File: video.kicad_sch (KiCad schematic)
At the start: 36 parts, among them CN10 COMPOSITE, CN9 VIDEO_DB23M, U4 DENISE, U40 74LS245, U41 74LS245, U94 74HCT14

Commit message: DRAM chips replaced with SIMM module
Added logic to decode 2MB chip + 1.5MB slow
Rewired trapdoor slot
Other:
- title: Rämixx500 -> Rämixx500_max
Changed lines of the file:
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@@
 	(paper "A3")
 	(title_block
-		(title "Rämixx500")
-		(date "2021-05-22")
-		(rev "1")
+		(title "Rämixx500_max")
+		(date "2026-03-13")
+		(rev "2")
 		(company "SukkoPera")
 		(comment 1 "DENISE IS PRETTY MUCH INTO VIDEO...")

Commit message: Completed routing, no DRC errors (but still a lot of warnings)
TODO: thoroughly review all small schematic changes
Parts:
- JP11: now left out of the parts list
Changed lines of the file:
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@@
 	(title_block
 		(title "Rämixx500_max")
-		(date "2026-03-13")
-		(rev "2")
+		(date "2026-03-25")
+		(rev "3")
 		(company "SukkoPera")
 		(comment 1 "DENISE IS PRETTY MUCH INTO VIDEO...")
@@
 		(unit 1)
 		(exclude_from_sim no)
-		(in_bom yes)
+		(in_bom no)
 		(on_board yes)
 		(dnp no)

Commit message: Started cleaning up BOM
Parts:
- JP99H1, JP99V1: now left out of the parts list
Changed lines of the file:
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@@
 		(unit 1)
 		(exclude_from_sim no)
-		(in_bom yes)
+		(in_bom no)
 		(on_board yes)
 		(dnp no)
@@
 		(unit 1)
 		(exclude_from_sim no)
-		(in_bom yes)
+		(in_bom no)
 		(on_board yes)
 		(dnp no)

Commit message: Working on BOM
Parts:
- C4, C40, C41: MFG Part Num C412C334M5U5TA -> C440C334K5R5TA7200; Mouser (none) -> 80-C440C334K5R-TR
- C401, C402: MFG Part Num EEUFR1C102 -> ECA-1EM102; Mouser (none) -> 667-ECA-1EM102
- C403, HY2: now not fitted
- C94: MFG Name (none) -> VISHAY; MFG Part Num (none) -> A104K15X7RF5TAA; Mouser (none) -> 594-A104K15X7RF5TAA
- CN10: MFG Name (none) -> SWITCHCRAFT; MFG Part Num (none) -> PJRAN1X1U01AUX; Mouser (none) -> 502-PJRAN1X1U01AUX
- CN9: MFG Name (none) -> COMMODORE; MFG Part Num (none) -> 390242-03
- HY1: MFG Name SKIP -> COMMODORE; MFG Part Num SKIP -> 390229-03

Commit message: more work on BOM done
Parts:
- E406: Mouser (none) -> 81-DSS1NB32A103Q91A
- R402, R403, R404: MFG Name (none) -> YAGEO; MFG Part Num (none) -> MFR-25FBF52-4K7; Mouser (none) -> 603-MFR-25FBF52-4K7
- R405: MFG Name (none) -> VISHAY; MFG Part Num (none) -> PR02000204707JA100; Mouser (none) -> 594-PR02000204707JA1
- R406: MFG Name (none) -> VISHAY; MFG Part Num (none) -> PR02000204708JA100; Mouser (none) -> 594-5083NW4R700JA100
- R409: MFG Name (none) -> YAGEO; MFG Part Num (none) -> MFR-25FBF52-150R; Mouser (none) -> 603-MFR-25FBF52-150R
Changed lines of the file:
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@@
 			)
 		)
-		(property "Mouser" ""
+		(property "Mouser" "603-MFR-25FBF52-4K7 "
+			(at 293.751 197.104 90)
+			(effects
+				(font
+					(size 1.27 1.27)
+				)
+				(hide yes)
+			)
+		)
+		(property "MFG Name" "YAGEO"
+			(at 293.751 197.104 90)
+			(effects
+				(font
+					(size 1.27 1.27)
+				)
+				(hide yes)
+			)
+		)
+		(property "MFG Part Num" "MFR-25FBF52-4K7 "
 			(at 293.751 197.104 90)
 			(effects
@@
 			)
 		)
-		(property "Mouser" ""
+		(property "Mouser" " 81-DSS1NB32A103Q91A "
 			(at 87.63 182.88 0)
 			(effects
@@
 			)
 		)
-		(property "Mouser" ""
+		(property "Mouser" "603-MFR-25FBF52-4K7 "
+			(at 323.723 79.248 90)
+			(effects
+				(font
+					(size 1.27 1.27)
+				)
+				(hide yes)
+			)
+		)
+		(property "MFG Name" "YAGEO"
+			(at 323.723 79.248 90)
+			(effects
+				(font
+					(size 1.27 1.27)
+				)
+				(hide yes)
+			)
+		)
+		(property "MFG Part Num" "MFR-25FBF52-4K7 "
 			(at 323.723 79.248 90)
 			(effects
@@
 			)
 		)
-		(property "Mouser" ""
+		(property "Mouser" "603-MFR-25FBF52-4K7 "
+			(at 328.549 79.121 90)
+			(effects
+				(font
+					(size 1.27 1.27)
+				)
+				(hide yes)
+			)
+		)
+		(property "MFG Name" "YAGEO"
+			(at 328.549 79.121 90)
+			(effects
+				(font
+					(size 1.27 1.27)
+				)
+				(hide yes)
+			)
+		)
+		(property "MFG Part Num" "MFR-25FBF52-4K7 "
 			(at 328.549 79.121 90)
 			(effects
@@
 			)
 		)
-		(property "Mouser" ""
+		(property "Mouser" "594-5083NW4R700JA100"
+			(at 119.38 193.04 90)
+			(effects
+				(font
+					(size 1.27 1.27)
+				)
+				(hide yes)
+			)
+		)
+		(property "MFG Name" "VISHAY"
+			(at 119.38 193.04 90)
+			(effects
+				(font
+					(size 1.27 1.27)
+				)
+				(hide yes)
+			)
+		)
+		(property "MFG Part Num" "PR02000204708JA100 "
 			(at 119.38 193.04 90)
 			(effects
@@
 			)
 		)
-		(property "Mouser" ""
+		(property "Mouser" "594-PR02000204707JA1 "
+			(at 255.905 193.04 90)
+			(effects
+				(font
+					(size 1.27 1.27)
+				)
+				(hide yes)
+			)
+		)
+		(property "MFG Name" "VISHAY"
+			(at 255.905 193.04 90)
+			(effects
+				(font
+					(size 1.27 1.27)
+				)
+				(hide yes)
+			)
+		)
+		(property "MFG Part Num" "PR02000204707JA100"
 			(at 255.905 193.04 90)
 			(effects
@@
 			)
 		)
-		(property "Mouser" ""
+		(property "Mouser" "603-MFR-25FBF52-150R"
 			(at 247.396 106.553 0)
 			(effects
+				(font
+					(size 1.27 1.27)
+				)
+				(hide yes)
+			)
+		)
+		(property "MFG Name" "YAGEO"
+			(at 247.396 106.553 0)
+			(effects
+				(font
+					(size 1.27 1.27)
+				)
+				(hide yes)
+			)
+		)
+		(property "MFG Part Num" "MFR-25FBF52-150R"
+			(at 247.396 106.553 0)
+			(effects

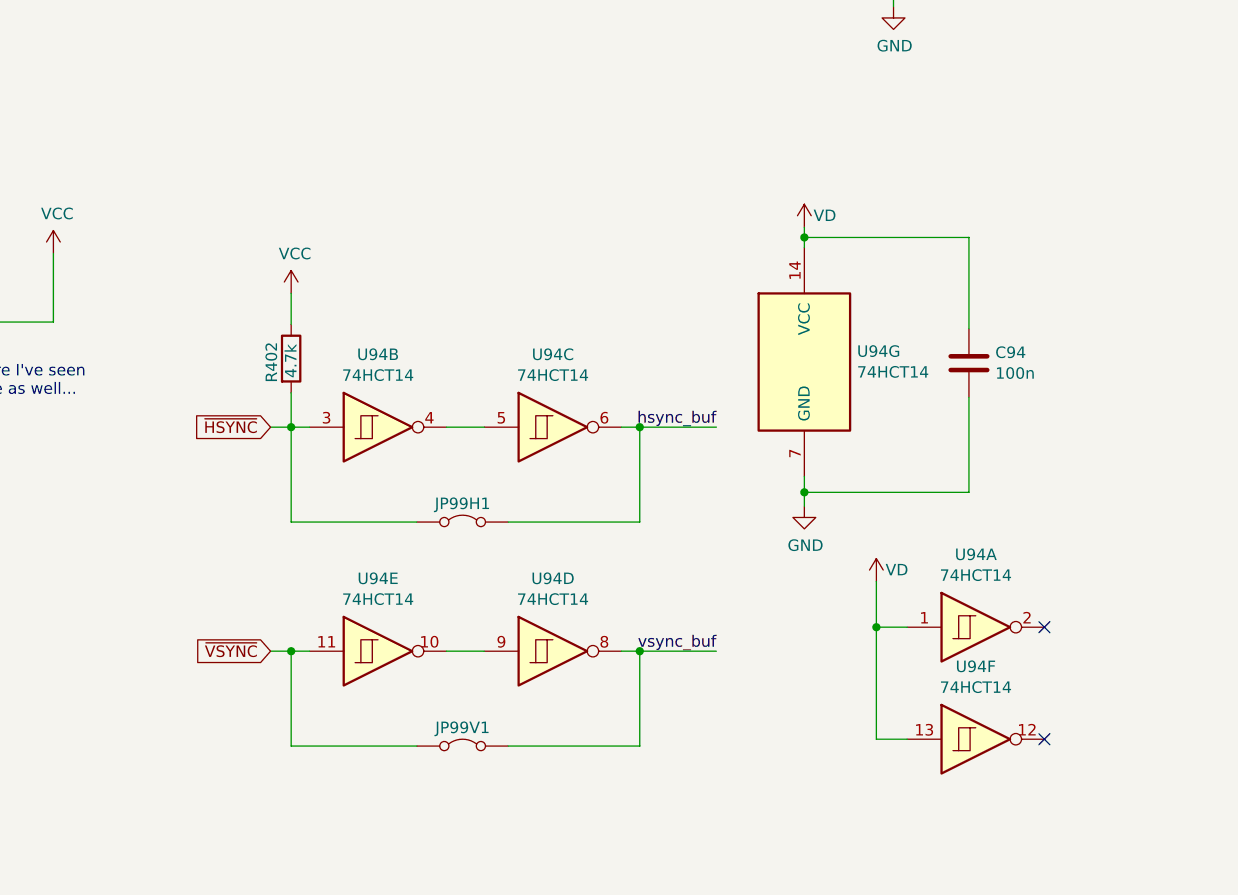
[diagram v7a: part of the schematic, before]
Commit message: More BOM work
I am marking optional components as DNP to get some overview
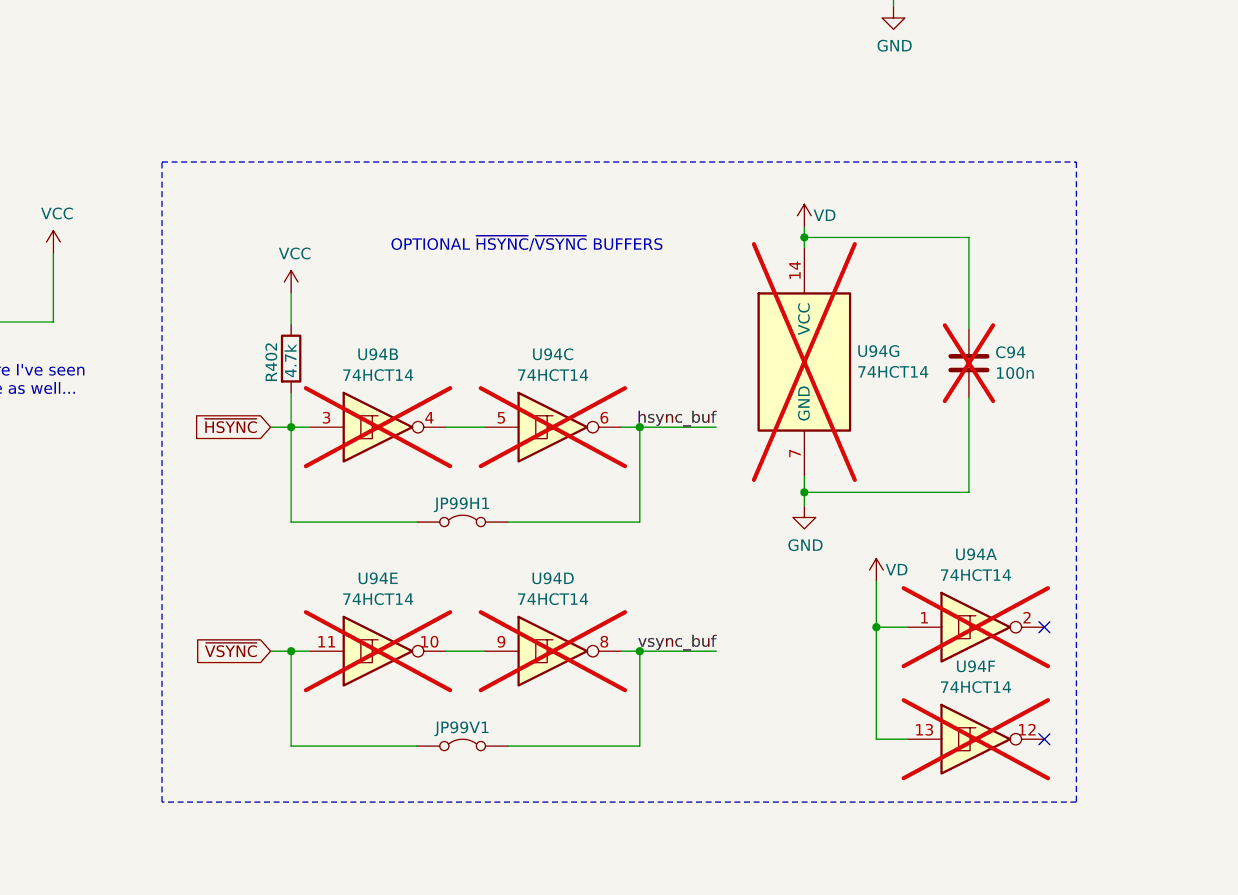
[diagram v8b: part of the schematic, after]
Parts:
- C94, U94: now not fitted
- E402, E434: Mouser (none) -> 81-DSS1NB32A151Q91A
- E403, E404, E405: Mouser (none) -> 81-DSS1NB32A103Q91A
- E406: Mouser 81-DSS1NB32A103Q91A -> 81-DSS1NB32A103Q91A
- E431, E432, E433, E435: MFG Name MURATA -> ABRACON; MFG Part Num BL02RN2R1M2B -> ALFB-02; Mouser (none) -> 815-ALFB-02
- U4: MFG Name (none) -> COMMODORE
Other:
- note added: "OPTIONAL ~{HSYNC}/~{VSYNC} BUFFERS"
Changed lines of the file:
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@@
 		(comment 4 "Licensed under CC BY-NC-SA 4.0")
 	)
+	(rectangle
+		(start 279.4 175.26)
+		(end 381 246.38)
+		(stroke
+			(width 0)
+			(type dash)
+		)
+		(fill
+			(type none)
+		)
+	)
 	(text "VIDEO POWER"
 		(exclude_from_sim no)
@@
 		)
 	)
+	(text "OPTIONAL ~{HSYNC}/~{VSYNC} BUFFERS"
+		(exclude_from_sim no)
+		(at 304.8 185.42 0)
+		(effects
+			(font
+				(size 1.27 1.27)
+				(thickness 0.1588)
+			)
+			(justify left bottom)
+		)
+	)
 	(text "I'm pretty sure I've seen\n4.7 used here as well..."
 		(exclude_from_sim no)
@@
 			)
 		)
+		(property "MFG Name" "COMMODORE"
+			(at 87.249 92.075 0)
+			(effects
+				(font
+					(size 1.27 1.27)
+				)
+				(hide yes)
+			)
+		)
 		(pin "5"
 		)
@@
 			)
 		)
-		(property "Mouser" ""
+		(property "Mouser" "81-DSS1NB32A103Q91A "
 			(at 372.237 80.899 0)
 			(effects
@@
 			)
 		)
-		(property "Mouser" ""
+		(property "Mouser" "81-DSS1NB32A103Q91A "
 			(at 366.522 62.103 0)
 			(effects
@@
 			)
 		)
-		(property "Mouser" ""
+		(property "Mouser" "81-DSS1NB32A103Q91A "
 			(at 369.316 71.247 0)
 			(effects
@@
 			)
 		)
-		(property "Mouser" ""
+		(property "Mouser" "81-DSS1NB32A151Q91A "
 			(at 330.2 150.876 0)
 			(effects
@@
 			)
 		)
-		(property "Mouser" ""
+		(property "Mouser" "81-DSS1NB32A151Q91A "
 			(at 341.884 62.738 0)
 			(effects
@@
 			)
 		)
+		(property "MFG Name" "COMMODORE"
+			(at 90.17 207.01 0)
+			(effects
+				(font
+					(size 1.27 1.27)
+				)
+				(hide yes)
+			)
+		)
 		(pin "42"
 		)
@@
 			)
 		)
-		(property "Mouser" " 81-DSS1NB32A103Q91A "
+		(property "Mouser" "81-DSS1NB32A103Q91A "
 			(at 87.63 182.88 0)
 			(effects
@@
 			)
 		)
-		(property "MFG Name" "MURATA"
+		(property "MFG Name" "ABRACON"
 			(at 307.34 128.651 0)
 			(effects
@@
 			)
 		)
-		(property "MFG Part Num" "BL02RN2R1M2B"
+		(property "MFG Part Num" "ALFB-02 "
 			(at 307.34 128.651 0)
 			(effects
@@
 			)
 		)
-		(property "Mouser" ""
+		(property "Mouser" "815-ALFB-02 "
 			(at 307.34 128.651 0)
 			(effects
@@
 			)
 		)
-		(property "MFG Name" "MURATA"
+		(property "MFG Name" "ABRACON"
 			(at 307.34 138.811 0)
 			(effects
@@
 			)
 		)
-		(property "MFG Part Num" "BL02RN2R1M2B"
+		(property "MFG Part Num" "ALFB-02 "
 			(at 307.34 138.811 0)
 			(effects
@@
 			)
 		)
-		(property "Mouser" ""
+		(property "Mouser" "815-ALFB-02 "
 			(at 307.34 138.811 0)
 			(effects
@@
 			)
 		)
-		(property "MFG Name" "MURATA"
+		(property "MFG Name" "ABRACON"
 			(at 290.83 133.731 0)
 			(effects
@@
 			)
 		)
-		(property "MFG Part Num" "BL02RN2R1M2B"
+		(property "MFG Part Num" "ALFB-02 "
 			(at 290.83 133.731 0)
 			(effects
@@
 			)
 		)
-		(property "Mouser" ""
+		(property "Mouser" "815-ALFB-02 "
 			(at 290.83 133.731 0)
 			(effects
@@
 			)
 		)
-		(property "MFG Name" "MURATA"
+		(property "MFG Name" "ABRACON"
 			(at 231.648 103.505 0)
 			(effects
@@
 			)
 		)
-		(property "MFG Part Num" "BL02RN2R1M2B"
+		(property "MFG Part Num" "ALFB-02 "
 			(at 231.648 103.505 0)
 			(effects
@@
 			)
 		)
-		(property "Mouser" ""
+		(property "Mouser" "815-ALFB-02 "
 			(at 231.648 103.505 0)
 			(effects
@@
 		(in_bom yes)
 		(on_board yes)
-		(dnp no)
+		(dnp yes)
 		(property "Reference" "U94"
 			(at 369.824 218.8972 0)
@@
 		(in_bom yes)
 		(on_board yes)
-		(dnp no)
+		(dnp yes)
 		(property "Reference" "U94"
 			(at 303.403 196.6722 0)
@@
 		(in_bom yes)
 		(on_board yes)
-		(dnp no)
+		(dnp yes)
 		(property "Reference" "U94"
 			(at 322.834 196.6722 0)
@@
 		(in_bom yes)
 		(on_board yes)
-		(dnp no)
+		(dnp yes)
 		(property "Reference" "U94"
 			(at 322.834 221.5642 0)
@@
 		(in_bom yes)
 		(on_board yes)
-		(dnp no)
+		(dnp yes)
 		(property "Reference" "U94"
 			(at 303.403 221.5642 0)
@@
 		(in_bom yes)
 		(on_board yes)
-		(dnp no)
+		(dnp yes)
 		(property "Reference" "U94"
 			(at 369.824 231.3432 0)
@@
 		(in_bom yes)
 		(on_board yes)
-		(dnp no)
+		(dnp yes)
 		(property "Reference" "U94"
 			(at 356.616 196.3166 0)
@@
 		(in_bom yes)
 		(on_board yes)
-		(dnp no)
+		(dnp yes)
 		(property "Reference" "C94"
 			(at 371.983 196.4436 0)
